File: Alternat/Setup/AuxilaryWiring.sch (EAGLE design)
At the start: 6 parts

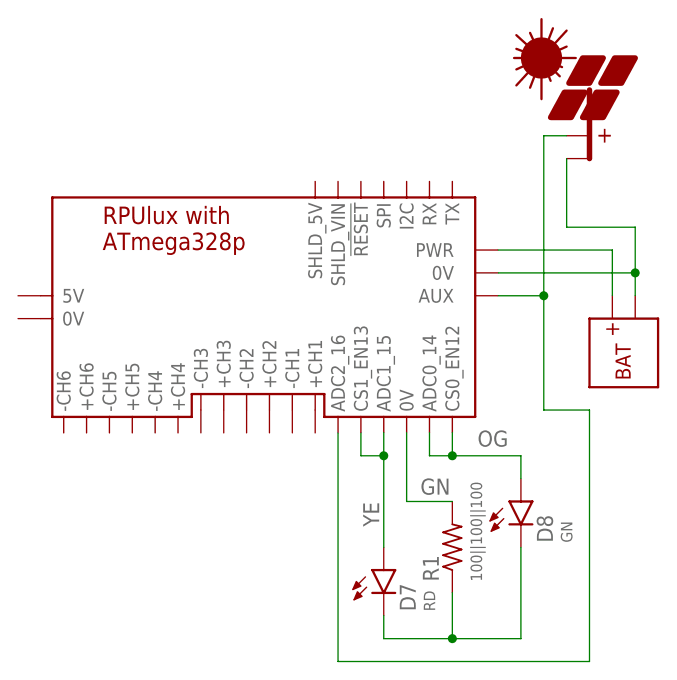
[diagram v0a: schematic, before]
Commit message: SelfTest: LED channels are running at half curr
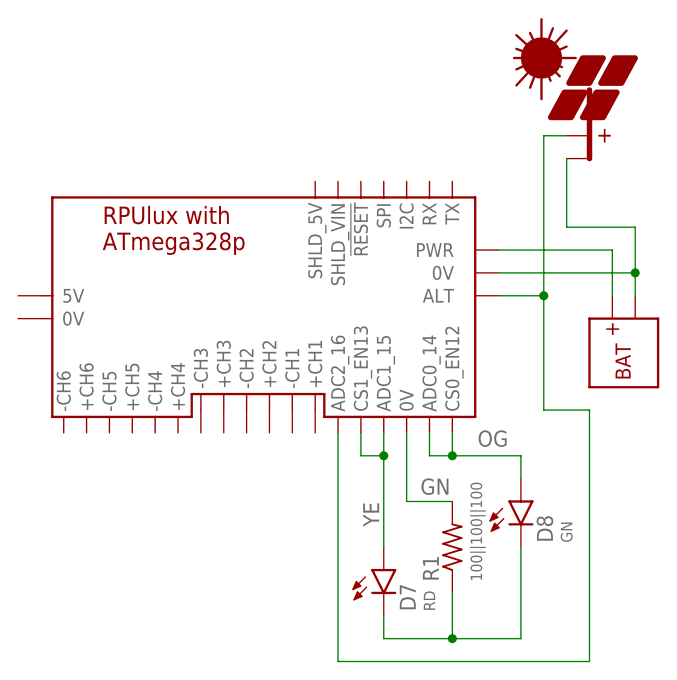
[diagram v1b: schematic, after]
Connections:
- net N$50: now also U$1.ALT; no longer U$1.AUX
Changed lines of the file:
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@@
 <wire x1="71.12" y1="109.22" x2="71.12" y2="127" width="0.1524" layer="91"/>
 <wire x1="71.12" y1="127" x2="73.66" y2="127" width="0.1524" layer="91"/>
-<pinref part="U$1" gate="G$1" pin="AUX"/>
+<pinref part="U$1" gate="G$1" pin="ALT"/>
 <wire x1="71.12" y1="109.22" x2="66.04" y2="109.22" width="0.1524" layer="91"/>
 <pinref part="U$1" gate="G$1" pin="ADC2_16"/>
